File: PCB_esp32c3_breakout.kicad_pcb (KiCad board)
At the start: 2 copper layers, 19.6 x 44.5 mm, 4 parts, among them J1 Conn_01x09_Pin, J2 Conn_01x09_Pin, U1 ESP32-C3-WROOM-02

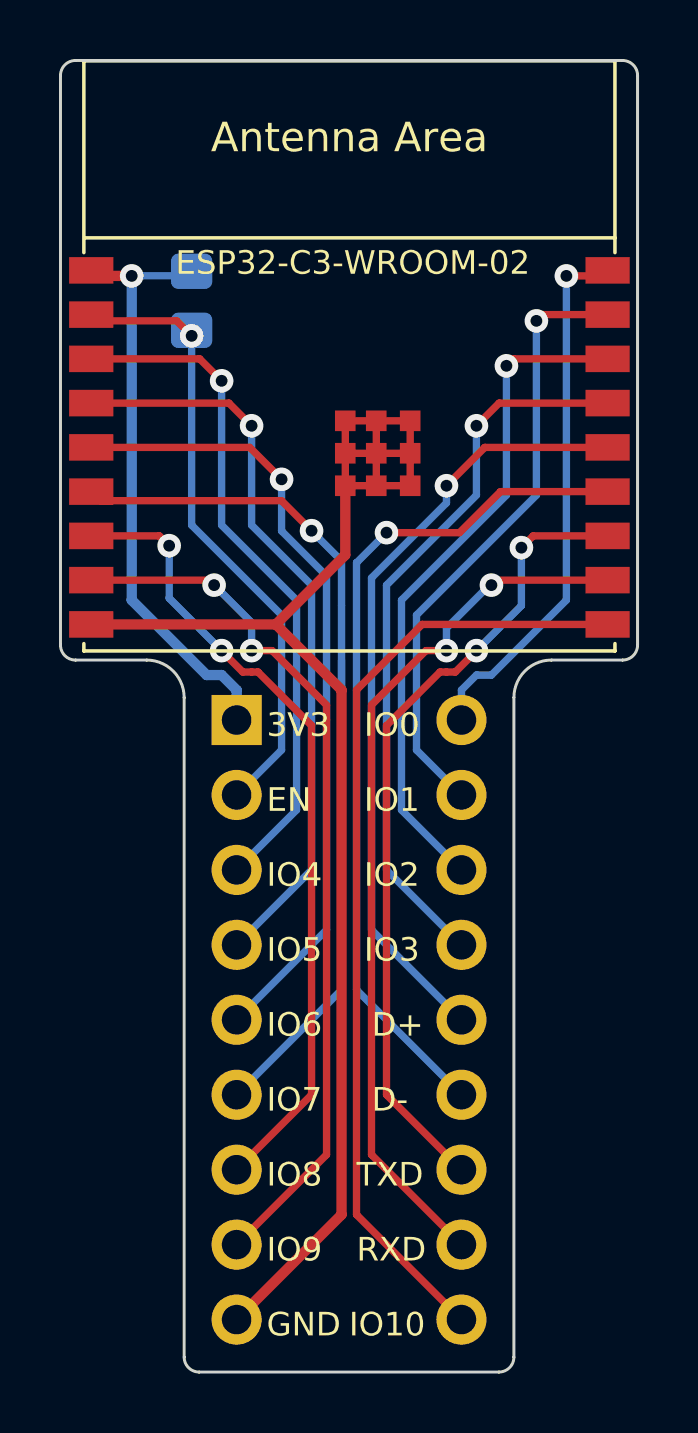
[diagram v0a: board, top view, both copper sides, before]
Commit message: Update PCB to Rev. 1.1
4層基板に変更。
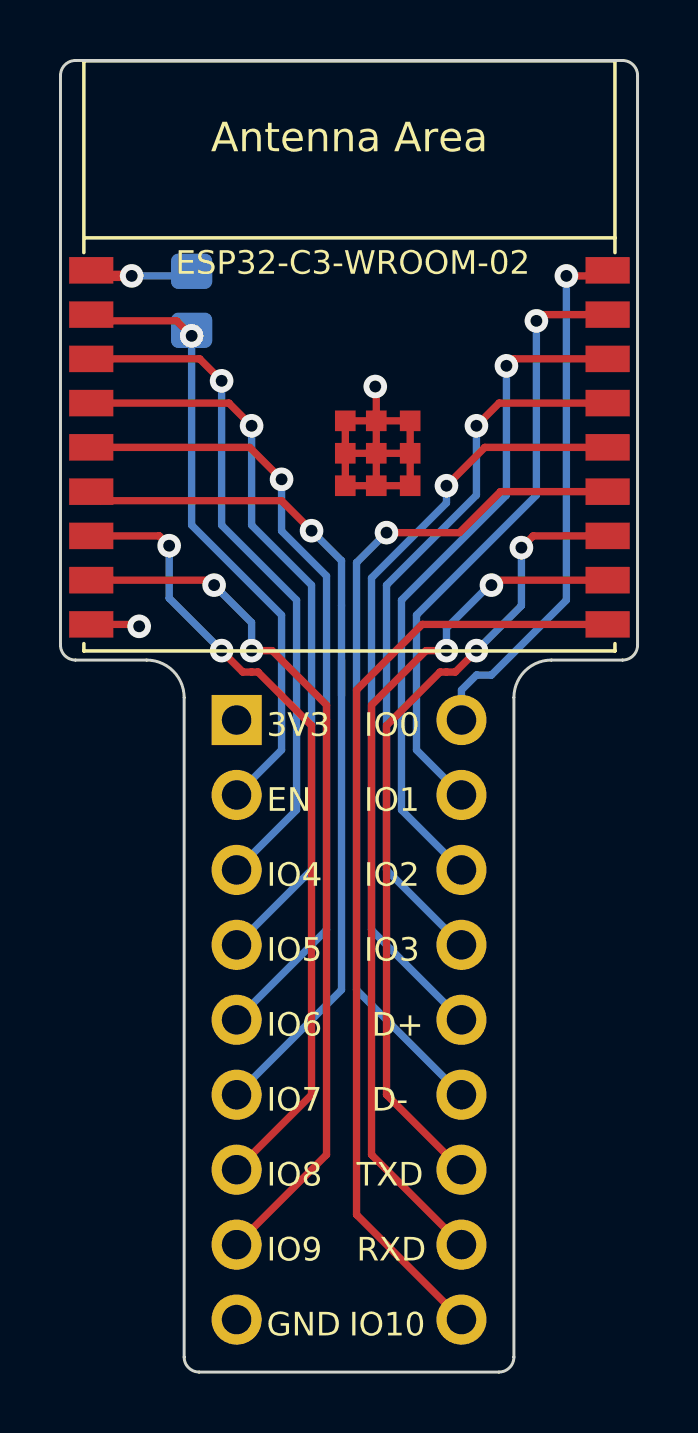
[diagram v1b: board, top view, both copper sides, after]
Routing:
- net GND: track 51.1 -> 16.0 mm, vias 0 -> 2
- net +3.3V: track 20.6 -> 3.81 mm
- added copper zone on In1.Cu, net +3.3V
- added copper zone on In2.Cu, net GND
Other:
- copper layers 2 -> 4
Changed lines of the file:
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@@
   (title_block
     (title "ESP32-C3-WROOM-02 Breakout Board")
-    (date "2024-02-10")
-    (rev "1")
+    (date "2024-02-11")
+    (rev "1.1")
     (company "K.Takata")
   )
   (layers
     (0 "F.Cu" signal)
+    (1 "In1.Cu" signal)
+    (2 "In2.Cu" signal)
     (31 "B.Cu" signal)
     (32 "B.Adhes" user "B.Adhesive")
@@
       (layer "F.Mask" (type "Top Solder Mask") (thickness 0.01))
       (layer "F.Cu" (type "copper") (thickness 0.035))
-      (layer "dielectric 1" (type "core") (thickness 1.51) (material "FR4") (epsilon_r 4.5) (loss_tangent 0.02))
+      (layer "dielectric 1" (type "prepreg") (thickness 0.1) (material "FR4") (epsilon_r 4.5) (loss_tangent 0.02))
+      (layer "In1.Cu" (type "copper") (thickness 0.035))
+      (layer "dielectric 2" (type "core") (thickness 1.24) (material "FR4") (epsilon_r 4.5) (loss_tangent 0.02))
+      (layer "In2.Cu" (type "copper") (thickness 0.035))
+      (layer "dielectric 3" (type "prepreg") (thickness 0.1) (material "FR4") (epsilon_r 4.5) (loss_tangent 0.02))
       (layer "B.Cu" (type "copper") (thickness 0.035))
       (layer "B.Mask" (type "Bottom Solder Mask") (thickness 0.01))
@@
   )
   (dimension (type aligned) (layer "Dwgs.User")
-    (pts (xy 69.863 38.62) (xy 69.85 83.058))
+    (pts (xy 69.85 38.608) (xy 69.85 83.058))
     (height 11.728022)
-    (gr_text "44.4380 mm" (at 56.978479 60.835233 89.98323855) (layer "Dwgs.User")
+    (gr_text "44.4500 mm" (at 56.971978 60.833 90) (layer "Dwgs.User")
       (effects (font (size 1 1) (thickness 0.15)))
     )
@@
   (segment (start 60.925 45.908) (end 61.113 45.72) (width 0.25) (layer "F.Cu") (net 1))
   (via (at 62.484 45.908) (size 0.8) (drill 0.4) (layers "F.Cu" "B.Cu") (net 1))
-  (segment (start 65.024 59.436) (end 62.484 56.896) (width 0.35) (layer "B.Cu") (net 1))
-  (segment (start 62.484 56.896) (end 62.484 45.908) (width 0.35) (layer "B.Cu") (net 1))
-  (segment (start 66.04 59.944) (end 65.532 59.436) (width 0.35) (layer "B.Cu") (net 1))
   (segment (start 64.36 45.908) (end 64.516 45.752) (width 0.35) (layer "B.Cu") (net 1))
   (segment (start 62.484 45.908) (end 64.36 45.908) (width 0.25) (layer "B.Cu") (net 1))
-  (segment (start 66.04 60.96) (end 66.04 59.944) (width 0.35) (layer "B.Cu") (net 1))
-  (segment (start 65.532 59.436) (end 65.024 59.436) (width 0.35) (layer "B.Cu") (net 1))
   (segment (start 60.901 47.432) (end 61.113 47.22) (width 0.25) (layer "F.Cu") (net 2))
   (segment (start 60.821653 46.928653) (end 61.113 47.22) (width 0.25) (layer "F.Cu") (net 2))
@@
   (segment (start 66.548 57.658) (end 65.278 56.388) (width 0.25) (layer "B.Cu") (net 8))
   (segment (start 66.548 58.608) (end 66.548 57.658) (width 0.25) (layer "B.Cu") (net 8))
-  (segment (start 61.113 57.72) (end 67.372 57.72) (width 0.35) (layer "F.Cu") (net 9))
   (segment (start 71.923 53.02) (end 71.923 50.82) (width 0.25) (layer "F.Cu") (net 9))
-  (segment (start 69.723 55.369) (end 67.372 57.72) (width 0.35) (layer "F.Cu") (net 9))
-  (segment (start 69.596 59.944) (end 69.596 77.724) (width 0.35) (layer "F.Cu") (net 9))
-  (segment (start 69.596 77.724) (end 66.04 81.28) (width 0.35) (layer "F.Cu") (net 9))
-  (segment (start 67.372 57.72) (end 69.596 59.944) (width 0.35) (layer "F.Cu") (net 9))
-  (segment (start 69.723 53.02) (end 69.723 55.369) (width 0.35) (layer "F.Cu") (net 9))
+  (segment (start 61.113 57.72) (end 62.673 57.72) (width 0.25) (layer "F.Cu") (net 9))
   (segment (start 69.723 50.82) (end 69.723 53.02) (width 0.25) (layer "F.Cu") (net 9))
+  (segment (start 70.773 49.691) (end 70.739 49.657) (width 0.25) (layer "F.Cu") (net 9))
   (segment (start 69.723 51.92) (end 71.923 51.92) (width 0.25) (layer "F.Cu") (net 9))
+  (segment (start 62.673 57.72) (end 62.738 57.785) (width 0.25) (layer "F.Cu") (net 9))
   (segment (start 71.923 50.82) (end 69.723 50.82) (width 0.25) (layer "F.Cu") (net 9))
   (segment (start 69.723 53.02) (end 71.923 53.02) (width 0.25) (layer "F.Cu") (net 9))
+  (segment (start 70.773 50.82) (end 70.773 49.691) (width 0.25) (layer "F.Cu") (net 9))
   (segment (start 70.773 50.82) (end 70.773 53.02) (width 0.25) (layer "F.Cu") (net 9))
+  (via (at 70.739 49.657) (size 0.8) (drill 0.4) (layers "F.Cu" "B.Cu") (net 9))
+  (via (at 62.738 57.785) (size 0.8) (drill 0.4) (layers "F.Cu" "B.Cu") (net 9))
   (segment (start 72.328 57.72) (end 78.613 57.72) (width 0.25) (layer "F.Cu") (net 10))
   (segment (start 70.104 59.944) (end 72.328 57.72) (width 0.25) (layer "F.Cu") (net 10))
@@
   (segment (start 74.676 59.436) (end 77.216 56.896) (width 0.25) (layer "B.Cu") (net 18))
   (segment (start 73.66 60.96) (end 73.66 59.944) (width 0.25) (layer "B.Cu") (net 18))
+  (zone (net 1) (net_name "+3.3V") (layer "In1.Cu") (hatch edge 0.5)
+    (connect_pads (clearance 0.5))
+    (min_thickness 0.25) (filled_areas_thickness no)
+    (fill yes (thermal_gap 0.5) (thermal_bridge_width 0.5))
+    (polygon
+      (pts
+        (xy 60.3504 44.8818)
+        (xy 60.3504 58.3692)
+        (xy 64.7954 58.3692)
+        (xy 64.7954 82.55)
+        (xy 74.9554 82.55)
+        (xy 74.9554 58.3692)
+        (xy 79.375 58.3692)
+        (xy 79.375 44.8818)
+      )
+    )
+  )
+  (zone (net 9) (net_name "GND") (layer "In2.Cu") (hatch edge 0.5)
+    (priority 1)
+    (connect_pads (clearance 0.5))
+    (min_thickness 0.25) (filled_areas_thickness no)
+    (fill yes (thermal_gap 0.5) (thermal_bridge_width 0.5))
+    (polygon
+      (pts
+        (xy 60.3504 44.8818)
+        (xy 60.3504 58.3692)
+        (xy 64.7954 58.3692)
+        (xy 64.7954 82.55)
+        (xy 74.9554 82.55)
+        (xy 74.9554 58.3692)
+        (xy 79.375 58.3692)
+        (xy 79.375 44.8818)
+      )
+    )
+  )
 )
